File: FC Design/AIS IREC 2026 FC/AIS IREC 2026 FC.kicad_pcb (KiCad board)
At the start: 4 copper layers, 65.3 x 38 mm, 51 parts, among them IC1 ADXL314WBCPZ-RL, IC2 MT29F8G08ABACAWP-IT_C_TR, J1 USB4216-03-A, J2 EBAA-02-C, J3 Conn_01x08, J4 EBAA-02-C, J5 EBAA-02-C, J6 Conn_01x08, Q1 MMBT3906-TP, Q2 DMN2008LFU-7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

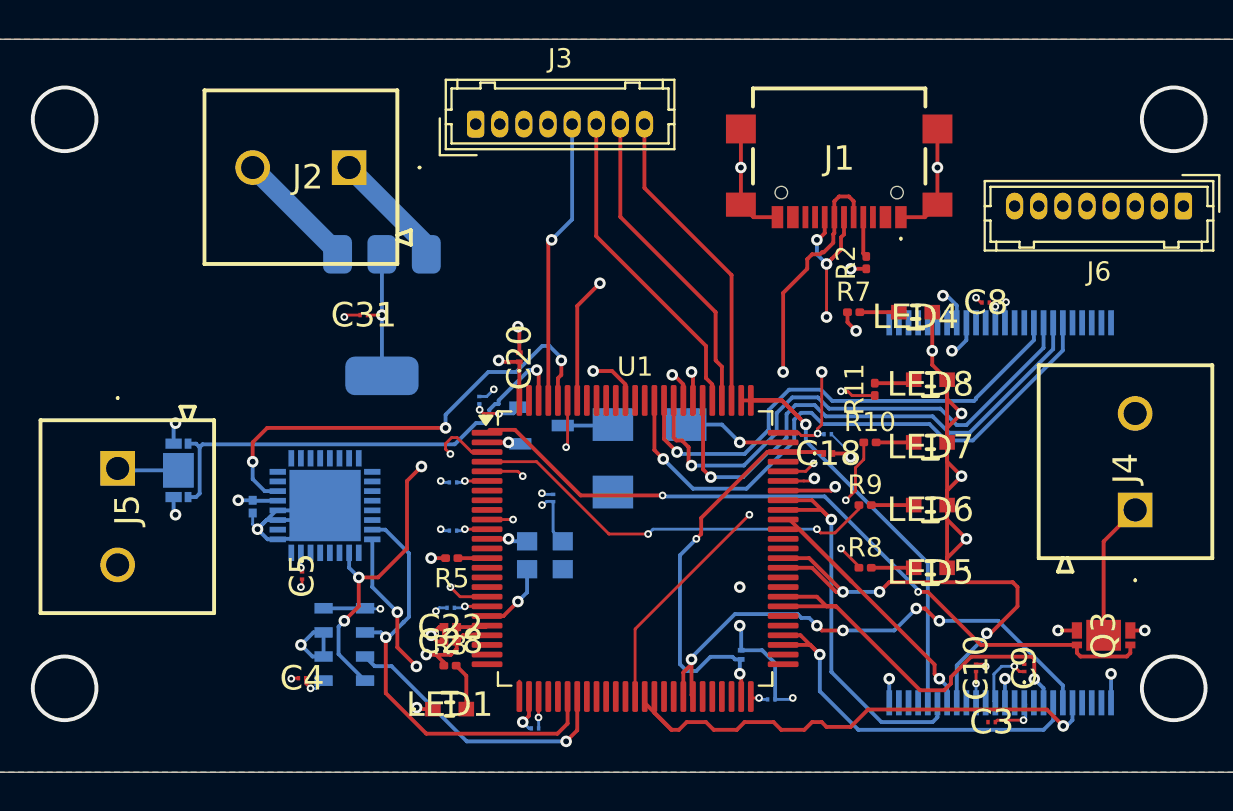
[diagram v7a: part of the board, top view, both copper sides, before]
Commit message: updated gerbers, BOM and placement files + component changes based off of JLC part availability
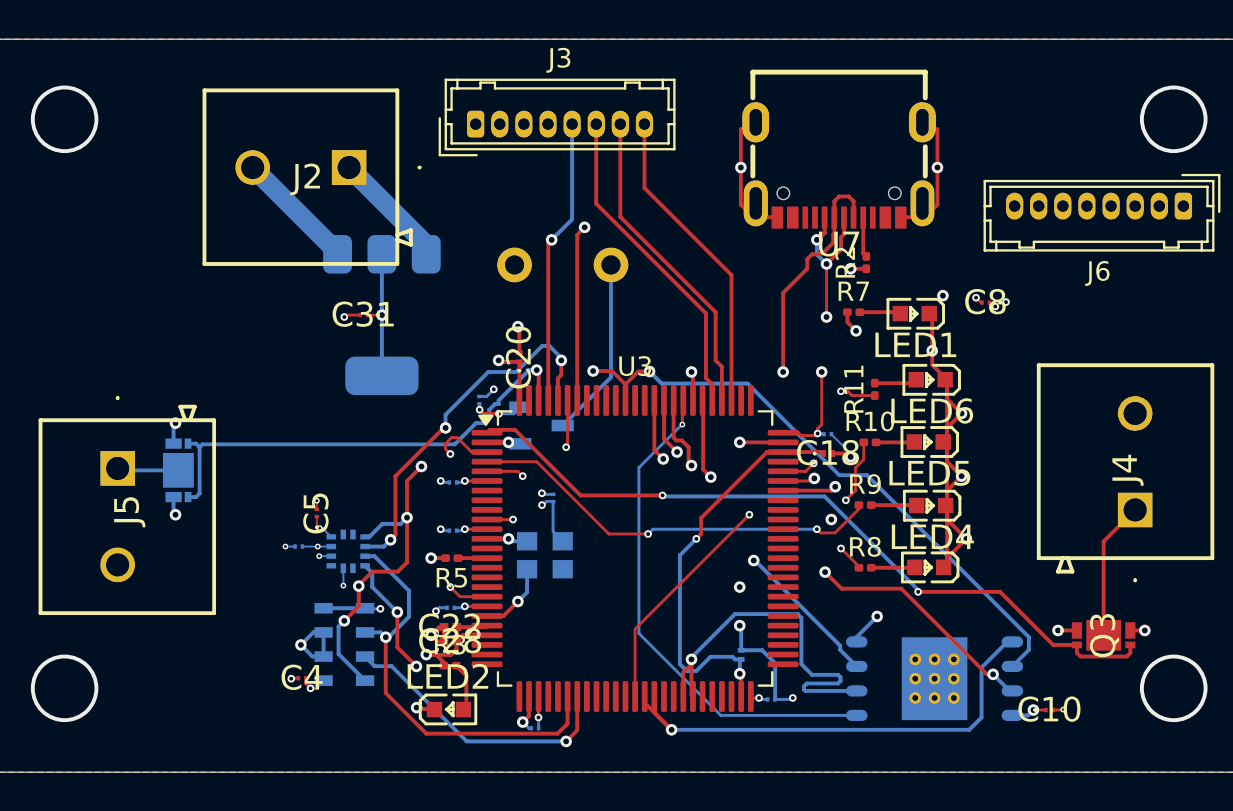
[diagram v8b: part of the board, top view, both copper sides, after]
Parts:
- removed C21: 1uF, SamacSys_Parts:CAPC0603X33N
- removed C3, C9: 100nF, SamacSys_Parts:GRM022C81C222KE01L
- removed IC1: ADXL314WBCPZ-RL, SamacSys_Parts:QFN50P500X500X155-33N-D
- removed IC2: MT29F8G08ABACAWP-IT_C_TR, SamacSys_Parts:SOP50P2000X120-48N
- removed J1: USB4216-03-A, SamacSys_Parts:USB421603A
- removed LED7, LED8: 598-8D91-127F, SamacSys_Parts:5988D91127F
- removed LS1: CSS-0578-SMT-TR, SamacSys_Parts:CSS0578SMTTR
- added BUZZER1: CY-9650-3029, JLC FOOTPRINT FILES:MLT-9650, B.Cu at (175.8, 35.3)
- added C2: 100nF, SamacSys_Parts:GRM022C81C222KE01L, B.Cu at (162.1, 49.9)
- added LED2: 0603 Green 509-620mcd, JLC FOOTPRINT FILES:LED0603-RD, F.Cu at (169.9, 58.4)
- added LED3: 0603 Green 509-620mcd, JLC FOOTPRINT FILES:LED0603-RD, F.Cu at (194.8, 51.0)
- added U3: STM32F205VGTx, Package_QFP:LQFP-100_14x14mm_P0.5mm, F.Cu at (179.6, 50.0)
- added U6: W25N01GVZEIG, JLC FOOTPRINT FILES:NAND FLASH, B.Cu at (195.1, 56.8)
- added U7: USB-310-B-SU, JLC FOOTPRINT FILES:USB 310F B, F.Cu at (190.2, 30.4)
- LED1, LED4, LED5, LED6: value 598-8D91-127F -> 0603 Green 509-620mcd; footprint SamacSys_Parts:5988D91127F -> JLC FOOTPRINT FILES:LED0603-RD
- U1: value STM32F205VBTx -> QMA6100P; footprint Package_QFP:LQFP-100_14x14mm_P0.5mm -> JLC FOOTPRINT FILES:MR ACCELEROMETER; moved to B.Cu
- moved LED1 31.7 mm to (194.1, 37.8), turned to 180 degrees
- moved U1 14.9 mm to (164.7, 50.1), turned to -90 degrees
- moved LED4 10.1 mm to (194.9, 47.8)
- moved LED5 6.53 mm to (194.8, 44.5)
- moved LED6 6.50 mm to (194.9, 41.2)
- moved C10 4.40 mm to (201.1, 58.4), turned to 0 degrees
- moved C5 3.33 mm to (163.1, 48.2), turned to 90 degrees
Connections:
- R10 pad 2: Net-(LED7-A) -> Net-(LED5-A)
- R11 pad 2: Net-(LED8-A) -> Net-(LED6-A)
- R3 pad 2: Net-(LED1-A) -> Net-(LED2-A)
- R5 pad 1: Net-(U1-NRST) -> Net-(U3-NRST)
- R7 pad 2: Net-(LED4-A) -> Net-(LED1-A)
- R8 pad 2: Net-(LED5-A) -> Net-(LED3-A)
- R9 pad 2: Net-(LED6-A) -> Net-(LED4-A)
- U1 pad 1: MAIN -> CLK
- U1 pad 10: GND -> 3.3V
- U1 pad 11: 3.3V -> unconnected-(U1-INT2-Pad11)
- U1 pad 12: OSC_CLK -> unconnected-(U1-INT1-Pad12)
- U1 pad 2: Buzzer control -> ACCELEROMETER CS
- U1 pad 3: INDICATOR 1 -> MISO
- U1 pad 4: INDICATOR 2 -> MOSI
- U1 pad 5: INDICATOR 3 -> unconnected-(U1-NC-Pad5)
- U1 pad 6: 3.3V -> GND
- U1 pad 8: unconnected-(U1-PC14-Pad8) -> GND
- U1 pad 9: unconnected-(U1-PC15-Pad9) -> 3.3V
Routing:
- net CLK: track 30.0 -> 60.1 mm, vias 4 -> 6
- net NAND4: track 24.4 -> 0.00 mm, vias 3 -> 0
- net ALE: track 27.8 -> 3.92 mm
- net NAND7: track 23.8 -> 0.00 mm, vias 1 -> 0
- net CLE: track 26.0 -> 2.95 mm
- net NAND3: track 21.2 -> 0.00 mm, vias 1 -> 0
- net NAND6: track 21.0 -> 0.00 mm, vias 1 -> 0
- net NAND2: track 20.4 -> 0.00 mm, vias 1 -> 0
- net GND: track 101.1 -> 83.1 mm
- net NAND5: track 17.9 -> 0.00 mm, vias 1 -> 0
- net WP: track 30.8 -> 18.2 mm, vias 1 -> 2
- net NAND EN: track 18.9 -> 26.1 mm, vias 2 -> 1
- net NAND1: track 27.7 -> 20.7 mm, vias 5 -> 1
- net Net-(BUZZER1-+): track 2.62 -> 9.36 mm
- net 3.3V: track 54.6 -> 47.9 mm, vias 26 -> 24
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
